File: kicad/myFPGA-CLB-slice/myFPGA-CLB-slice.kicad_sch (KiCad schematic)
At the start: 38 parts, among them J1 Conn_01x04, J10 Conn_01x02, J11 Conn_01x02, J12 Conn_01x04, J13 Conn_01x04, J14 Conn_01x04, J15 Conn_01x04, J2 Conn_01x04, J3 Conn_01x04, J4 Conn_01x04, J5 Conn_01x04, J6 Conn_01x04, J7 Conn_01x04, J8 Conn_01x02, J9 Conn_01x04, U1 NC7SB3157P6X, U2 74AHCT595

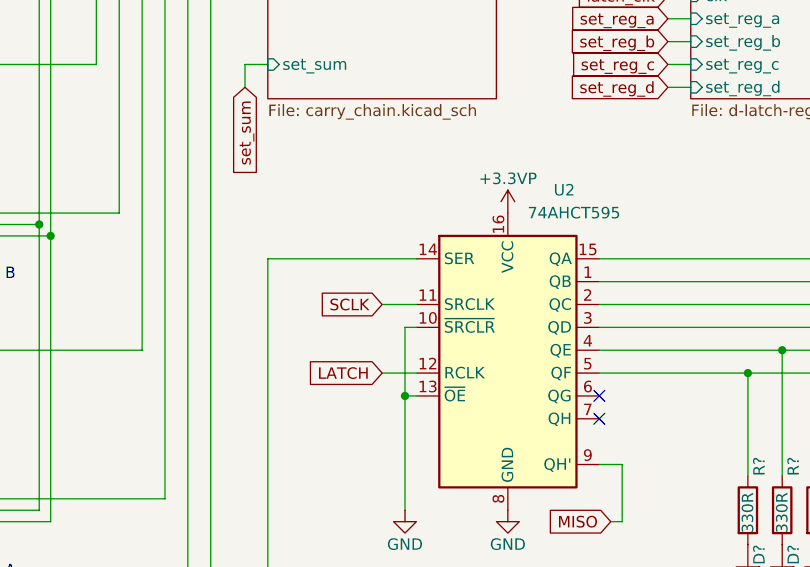
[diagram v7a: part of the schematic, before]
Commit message: gitignore fix
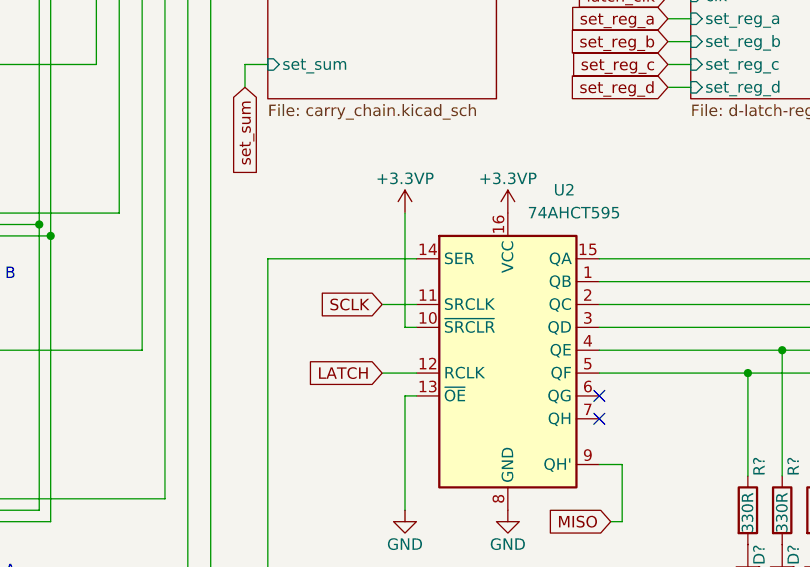
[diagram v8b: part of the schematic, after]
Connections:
- net +3.3VP: now also U2.10 (~{SRCLR})
- net GND: no longer U2.10 (~{SRCLR})
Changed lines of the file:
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@@
   (junction (at 107.95 43.18) (diameter 0) (color 0 0 0 0)
-  )
-  (junction (at 199.39 109.22) (diameter 0) (color 0 0 0 0)
   )
   (junction (at 160.02 91.44) (diameter 0) (color 0 0 0 0)
@@
     (stroke (width 0) (type default))
   )
-  (wire (pts (xy 199.39 101.6) (xy 199.39 109.22))
-    (stroke (width 0) (type default))
-  )
   (wire (pts (xy 107.95 43.18) (xy 115.57 43.18))
     (stroke (width 0) (type default))
@@
   )
   (wire (pts (xy 135.89 29.21) (xy 135.89 26.67))
+    (stroke (width 0) (type default))
+  )
+  (wire (pts (xy 199.39 88.9) (xy 199.39 101.6))
     (stroke (width 0) (type default))
   )
@@
         )
       )
+    )
+  )
+  (symbol (lib_id "power:+3.3VP") (at 199.39 88.9 0) (unit 1)
+    (in_bom yes) (on_board yes) (dnp no)
+    (property "Reference" "#PWR0152" (at 203.2 90.17 0)
+      (effects (font (size 1.27 1.27)) hide)
+    )
+    (property "Value" "+3.3VP" (at 199.39 85.09 0)
+      (effects (font (size 1.27 1.27)))
+    )
+    (property "Footprint" "" (at 199.39 88.9 0)
+      (effects (font (size 1.27 1.27)) hide)
+    )
+    (property "Datasheet" "" (at 199.39 88.9 0)
+      (effects (font (size 1.27 1.27)) hide)
+    )
+    (pin "1")
+    (instances
+      (project "myFPGA-CLB-slice"
+        (path "/2d29d97f-956a-4594-9321-3d88807a498d"
+          (reference "#PWR0152") (unit 1)
+        )
+      )
